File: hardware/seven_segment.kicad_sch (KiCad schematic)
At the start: 36 parts, among them J1 Conn_01x16, J2 PJ-102AH, J3 Conn_01x04, J5 Conn_01x06, SW2 SW_Push, U1 ESP32-WROOM-32E, U2 ULN2003A, U3 ULN2003A, U4 TPS562200, U5 74HC595, U6 74HC595, U7 ULN2003A

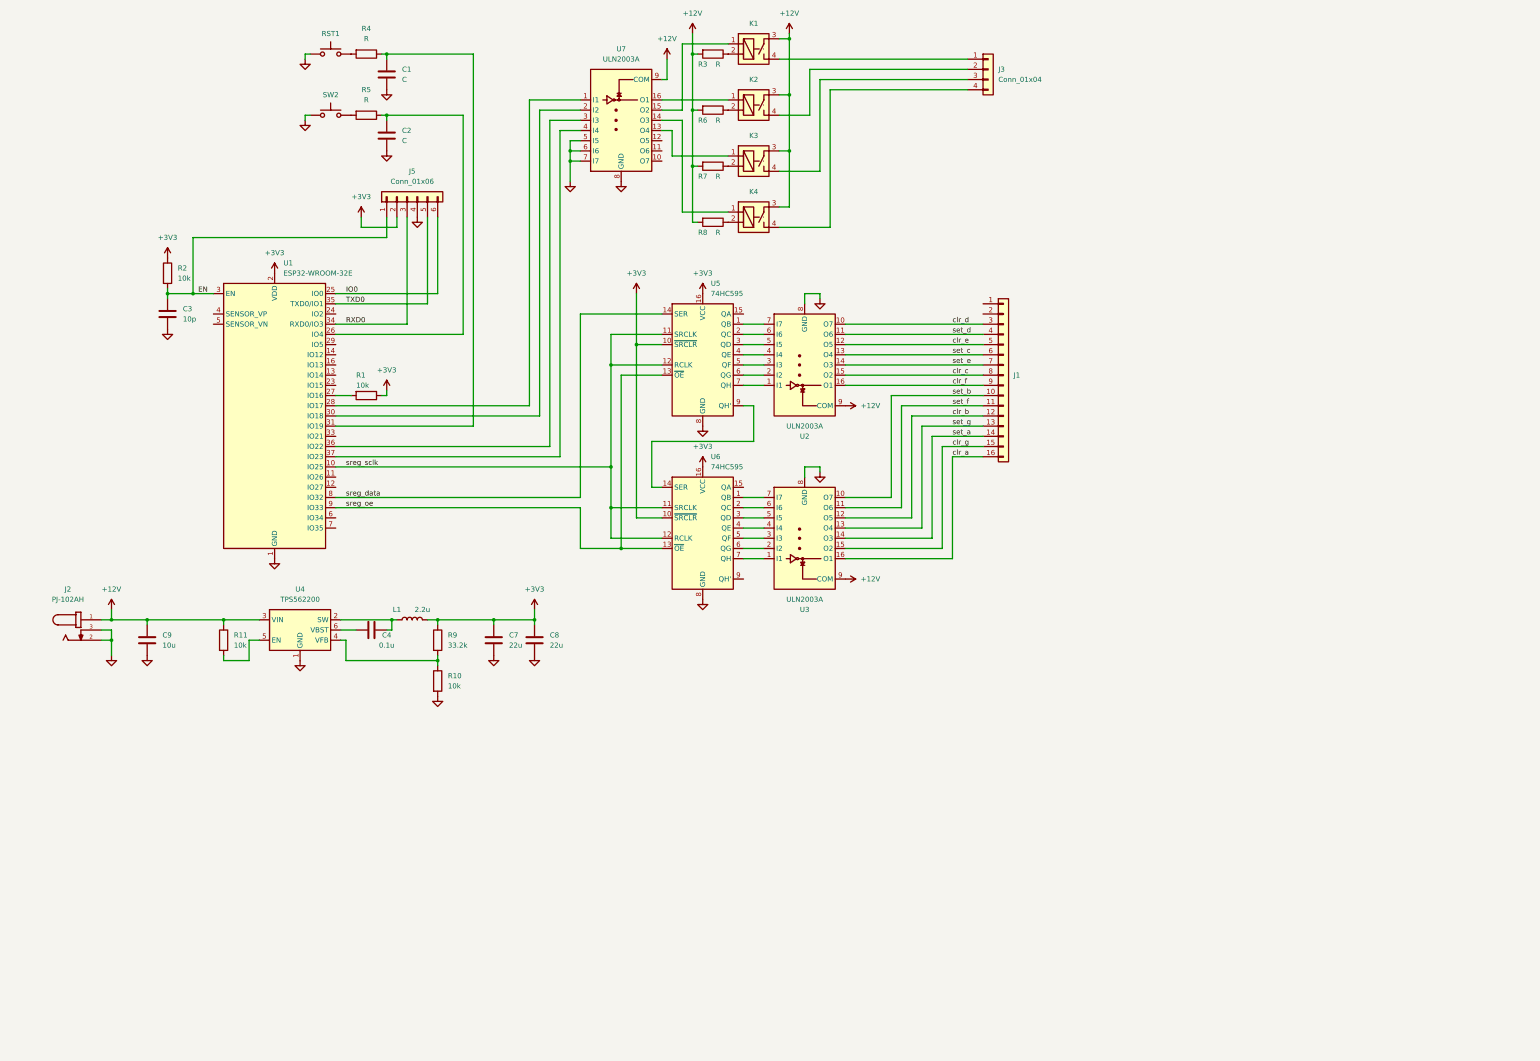
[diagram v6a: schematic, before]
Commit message: hardware: revision 4
Changelog:
Load switching:
        - Move back to transistors rather than relays since they are
          more reliable, faster and quiter.
Mechanics:
        - Ditch the hammond enclosure for a 3d-printed chassi.
        - Connectors are now located on the back-side of the PCB, the
          idea is to cut out holes in the display backside to pass
          through cables.
UI:
        - Add 2 LEDs
        - Remove a button
Power:
        - Remove 12V connector in favor of USB-C
        - Step up/down the required 12/3.3V from the USB 5V
Other:
        - Clean up repo structure
        - Remove unused libraries
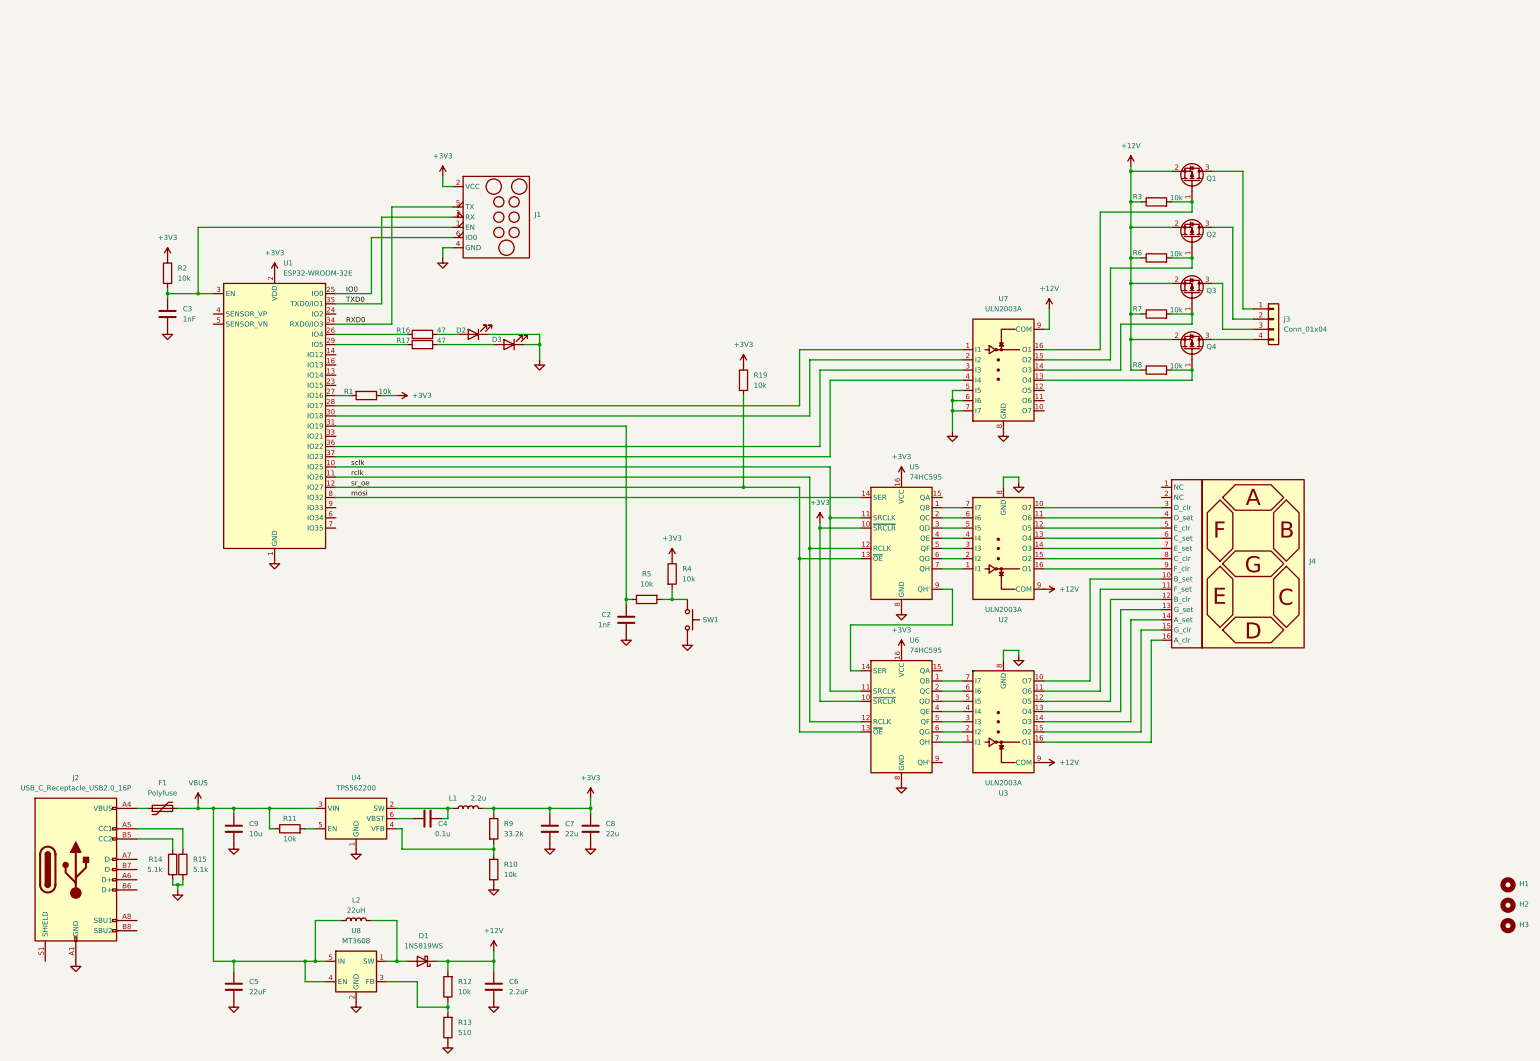
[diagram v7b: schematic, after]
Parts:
- removed C1: C, Resistor_SMD:R_0603_1608Metric, symbol Device:C
- removed J1: Conn_01x16, Connector_PinHeader_2.54mm:PinHeader_2x08_P2.54mm_Vertical, symbol Connector_Generic:Conn_01x16
- removed J2: PJ-102AH, PJ_102AH:CUI_PJ-102AH, symbol PJ-102AH:PJ-102AH
- removed J5: Conn_01x06, Connector:Tag-Connect_TC2030-IDC-NL_2x03_P1.27mm_Vertical, symbol Connector_Generic:Conn_01x06
- removed K1, K2, K3, K4: ~, 00_customfootprints:G6DN-1A-SL, symbol 00_customsymbols:Relay
- removed RST1: SW_Push, pushbutton:TO_6083716_WRE, symbol Switch:SW_Push
- added C5: 22uF, Capacitor_SMD:C_0805_2012Metric, symbol Device:C
- added C6: 2.2uF, Capacitor_SMD:C_1210_3225Metric, symbol Device:C
- added D1: 1N5819WS, Diode_SMD:D_SOD-323, symbol Diode:1N5819WS
- added D2, D3: LED, LED_SMD:LED_0603_1608Metric, symbol Device:LED
- added F1: Polyfuse, Resistor_SMD:R_1210_3225Metric, symbol Device:Polyfuse
- added H1, H2, H3: MountingHole, MountingHole:MountingHole_3mm, symbol Mechanical:MountingHole
- added J1: ~, Connector:Tag-Connect_TC2030-IDC-NL_2x03_P1.27mm_Vertical, symbol 00_custom:tagconnect-esp32
- added J2: USB_C_Receptacle_USB2.0_16P, Connector_USB:USB_C_Receptacle_GCT_USB4105-xx-A_16P_TopMnt_Horizontal, symbol Connector:USB_C_Receptacle_USB2.0_16P
- added J4: ~, Connector_PinHeader_2.54mm:PinHeader_2x08_P2.54mm_Vertical_SMD, symbol 00_custom:7-segment
- added L2: 22uH, Inductor_SMD:L_Bourns_SRN6045TA, symbol Device:L
- added Q1, Q2, Q3, Q4: IRLML5203, Package_TO_SOT_SMD:SOT-23, symbol Transistor_FET:IRLML5203
- added R12, R19: 10k, Resistor_SMD:R_0603_1608Metric, symbol Device:R
- added R13: 510, Resistor_SMD:R_0603_1608Metric, symbol Device:R
- added R14, R15: 5.1k, Resistor_SMD:R_0603_1608Metric, symbol Device:R
- added R16, R17: 47, Resistor_SMD:R_0603_1608Metric, symbol Device:R
- added U8: MT3608, Package_TO_SOT_SMD:SOT-23-6, symbol Regulator_Switching:MT3608
- C2: value C -> 1nF
- C3: value 10p -> 1nF
- R3, R4, R5, R6, R7, R8: value R -> 10k
- SW1: renamed from SW2; footprint pushbutton:TO_6083716_WRE -> Button_Switch_SMD:SW_SPST_CK_RS282G05A3
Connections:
- net +12V: now also R3.1, R6.1, R7.1, R8.1, C6.1, D1.1 (K), Q1.2 (S), Q2.2 (S), Q3.2 (S), Q4.2 (S), R12.2; no longer C9.1, R11.1, R3.2, R6.2, R7.2, R8.2, U4.3 (VIN)
- net +3V3: now also R4.1, J1.2 (VCC), R19.1
- net GND: now also C5.2, C6.2, D2.1 (K), D3.1 (K), J1.4 (GND), J2.A1 (GND), J2.A12 (GND), J2.B1 (GND), J2.B12 (GND), R13.1, R14.2, R15.2, U8.2 (GND)
- net IO0: now also J1.6 (IO0)
- net RXD0: now also J1.5 (TX)
- net TXD0: now also J1.3 (RX)
- net at U7.15 (O2): now also R6.2, Q2.1 (G)
- net at J3.1 (Pin_1): now also Q1.3 (D)
- net at U1.31 (IO19): now also C2.1, R5.1; no longer R4.1
- net at R4.2: now also R5.2, SW1.1
- net at J3.2 (Pin_2): now also Q2.3 (D)
- net at J3.3 (Pin_3): now also Q3.3 (D)
- net at J3.4 (Pin_4): now also Q4.3 (D)
- net at U7.13 (O4): now also R8.2, Q4.1 (G)
- net at U7.14 (O3): now also R7.2, Q3.1 (G)
- net at U7.16 (O1): now also R3.2, Q1.1 (G)
- net rclk: now reaches U1.11 (IO26)
- net rclk: now also U5.12 (RCLK), U6.12 (RCLK)
- net sr_oe: now reaches U1.12 (IO27)
- net sr_oe: now also U5.13 (~{OE}), U6.13 (~{OE}), R19.2
- net at U1.29 (IO5): now also R17.1
- net EN: no longer names the net of C3.1, R2.2, U1.3 (EN)
- net EN: now also J1.1 (EN)
- net clr_a: no longer names the net of U3.16 (O1)
- net clr_a: now also J4.16 (A_clr)
- net clr_b: no longer names the net of U3.12 (O5)
- net clr_b: now also J4.12 (B_clr)
- net clr_c: no longer names the net of U2.15 (O2)
- net clr_c: now also J4.8 (C_clr)
- net clr_d: no longer names the net of U2.10 (O7)
- net clr_d: now also J4.3 (D_clr)
- net clr_e: no longer names the net of U2.12 (O5)
- net clr_e: now also J4.5 (E_clr)
- net clr_f: no longer names the net of U2.16 (O1)
- net clr_f: now also J4.9 (F_clr)
- net clr_g: no longer names the net of U3.15 (O2)
- net clr_g: now also J4.15 (G_clr)
- net set_a: no longer names the net of U3.14 (O3)
- net set_a: now also J4.14 (A_set)
- net set_b: no longer names the net of U3.10 (O7)
- net set_b: now also J4.10 (B_set)
- net set_c: no longer names the net of U2.13 (O4)
- net set_c: now also J4.6 (C_set)
- net set_d: no longer names the net of U2.11 (O6)
- net set_d: now also J4.4 (D_set)
- net set_e: no longer names the net of U2.14 (O3)
- net set_e: now also J4.7 (E_set)
- net set_f: no longer names the net of U3.11 (O6)
- net set_f: now also J4.11 (F_set)
- net set_g: no longer names the net of U3.13 (O4)
- net set_g: now also J4.13 (G_set)
- net sreg_data renamed mosi
- removed net sreg_oe: U1.9 (IO33), U5.13 (~{OE}), U6.13 (~{OE})
- net sreg_sclk renamed sclk
- net sclk: no longer U5.12 (RCLK), U6.12 (RCLK)
- new net: D1.2 (A), L2.2, U8.1 (SW)
- new net: D2.2 (A), R16.2
- new net: R12.1, R13.2, U8.3 (FB)
- new net: J2.B5 (CC2), R14.1
- new net: F1.1, J2.A4 (VBUS), J2.A9 (VBUS), J2.B4 (VBUS), J2.B9 (VBUS)
- new net: R16.1, U1.26 (IO4)
- new net: D3.2 (A), R17.2
- new net: J2.A5 (CC1), R15.1
- new net VBUS: C5.1, C9.1, F1.2, L2.1, R11.1, U4.3 (VIN), U8.4 (EN), U8.5 (IN)
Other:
- moved on the sheet: C2, C4, C7, C8, C9, J3, L1, R10, R11, R5, R9, SW1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
